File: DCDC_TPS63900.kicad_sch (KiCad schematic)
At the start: 14 parts, among them U11 TPS63900

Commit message: Initial layout before routing.
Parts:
- renumbered C27 to C23, C28 to C24, C29 to C25, C30 to C26, C31 to C27, C32 to C28, C33 to C29, C34 to C30, R24 to R28, R25 to R29, R26 to R30, R27 to R31, U11 to U12

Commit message: PCB layout done, signal routing finished, power routing remaining.
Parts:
- renumbered R28 to R29, R29 to R30, R30 to R31, R31 to R32
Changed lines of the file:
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@@
 		(dnp no)
 		(fields_autoplaced yes)
-		(property "Reference" "R29"
+		(property "Reference" "R30"
 			(at 162.56 114.2999 0)
 			(show_name no)
@@
 			(project "DigiFur-Rev1.0"
 				(path "/47dbac06-588f-419b-91d0-b3790df884b4/3218340f-e986-4868-8421-14e8efd0ba88"
-					(reference "R29")
-					(unit 1)
-				)
-				(path "/47dbac06-588f-419b-91d0-b3790df884b4/88e4d8d5-9b78-4fb5-9f90-e7a9602950c7"
-					(reference "R37")
-					(unit 1)
-				)
-				(path "/47dbac06-588f-419b-91d0-b3790df884b4/a83537bf-b40b-4f0e-8d76-5aa1105fd7e8"
-					(reference "R33")
-					(unit 1)
-				)
-				(path "/47dbac06-588f-419b-91d0-b3790df884b4/b9f26843-1012-4a63-8c48-45d26c73c917"
-					(reference "R41")
+					(reference "R30")
+					(unit 1)
+				)
+				(path "/47dbac06-588f-419b-91d0-b3790df884b4/88e4d8d5-9b78-4fb5-9f90-e7a9602950c7"
+					(reference "R38")
+					(unit 1)
+				)
+				(path "/47dbac06-588f-419b-91d0-b3790df884b4/a83537bf-b40b-4f0e-8d76-5aa1105fd7e8"
+					(reference "R34")
+					(unit 1)
+				)
+				(path "/47dbac06-588f-419b-91d0-b3790df884b4/b9f26843-1012-4a63-8c48-45d26c73c917"
+					(reference "R42")
 					(unit 1)
 				)
@@
 		(dnp no)
 		(fields_autoplaced yes)
-		(property "Reference" "#PWR052"
+		(property "Reference" "#PWR053"
 			(at 142.24 129.54 0)
 			(hide yes)
@@
 			(project "DigiFur-Rev1.0"
 				(path "/47dbac06-588f-419b-91d0-b3790df884b4/3218340f-e986-4868-8421-14e8efd0ba88"
-					(reference "#PWR052")
-					(unit 1)
-				)
-				(path "/47dbac06-588f-419b-91d0-b3790df884b4/88e4d8d5-9b78-4fb5-9f90-e7a9602950c7"
+					(reference "#PWR053")
+					(unit 1)
+				)
+				(path "/47dbac06-588f-419b-91d0-b3790df884b4/88e4d8d5-9b78-4fb5-9f90-e7a9602950c7"
+					(reference "#PWR055")
+					(unit 1)
+				)
+				(path "/47dbac06-588f-419b-91d0-b3790df884b4/a83537bf-b40b-4f0e-8d76-5aa1105fd7e8"
 					(reference "#PWR054")
 					(unit 1)
 				)
-				(path "/47dbac06-588f-419b-91d0-b3790df884b4/a83537bf-b40b-4f0e-8d76-5aa1105fd7e8"
-					(reference "#PWR053")
-					(unit 1)
-				)
-				(path "/47dbac06-588f-419b-91d0-b3790df884b4/b9f26843-1012-4a63-8c48-45d26c73c917"
-					(reference "#PWR055")
+				(path "/47dbac06-588f-419b-91d0-b3790df884b4/b9f26843-1012-4a63-8c48-45d26c73c917"
+					(reference "#PWR056")
 					(unit 1)
 				)
@@
 		(dnp yes)
 		(fields_autoplaced yes)
-		(property "Reference" "R30"
+		(property "Reference" "R31"
 			(at 172.72 104.1399 0)
 			(show_name no)
@@
 			(project "DigiFur-Rev1.0"
 				(path "/47dbac06-588f-419b-91d0-b3790df884b4/3218340f-e986-4868-8421-14e8efd0ba88"
-					(reference "R30")
-					(unit 1)
-				)
-				(path "/47dbac06-588f-419b-91d0-b3790df884b4/88e4d8d5-9b78-4fb5-9f90-e7a9602950c7"
-					(reference "R38")
-					(unit 1)
-				)
-				(path "/47dbac06-588f-419b-91d0-b3790df884b4/a83537bf-b40b-4f0e-8d76-5aa1105fd7e8"
-					(reference "R34")
-					(unit 1)
-				)
-				(path "/47dbac06-588f-419b-91d0-b3790df884b4/b9f26843-1012-4a63-8c48-45d26c73c917"
-					(reference "R42")
+					(reference "R31")
+					(unit 1)
+				)
+				(path "/47dbac06-588f-419b-91d0-b3790df884b4/88e4d8d5-9b78-4fb5-9f90-e7a9602950c7"
+					(reference "R39")
+					(unit 1)
+				)
+				(path "/47dbac06-588f-419b-91d0-b3790df884b4/a83537bf-b40b-4f0e-8d76-5aa1105fd7e8"
+					(reference "R35")
+					(unit 1)
+				)
+				(path "/47dbac06-588f-419b-91d0-b3790df884b4/b9f26843-1012-4a63-8c48-45d26c73c917"
+					(reference "R43")
 					(unit 1)
 				)
@@
 		(dnp no)
 		(fields_autoplaced yes)
-		(property "Reference" "R28"
+		(property "Reference" "R29"
 			(at 162.56 104.1399 0)
 			(show_name no)
@@
 			(project "DigiFur-Rev1.0"
 				(path "/47dbac06-588f-419b-91d0-b3790df884b4/3218340f-e986-4868-8421-14e8efd0ba88"
-					(reference "R28")
-					(unit 1)
-				)
-				(path "/47dbac06-588f-419b-91d0-b3790df884b4/88e4d8d5-9b78-4fb5-9f90-e7a9602950c7"
-					(reference "R36")
-					(unit 1)
-				)
-				(path "/47dbac06-588f-419b-91d0-b3790df884b4/a83537bf-b40b-4f0e-8d76-5aa1105fd7e8"
-					(reference "R32")
-					(unit 1)
-				)
-				(path "/47dbac06-588f-419b-91d0-b3790df884b4/b9f26843-1012-4a63-8c48-45d26c73c917"
-					(reference "R40")
+					(reference "R29")
+					(unit 1)
+				)
+				(path "/47dbac06-588f-419b-91d0-b3790df884b4/88e4d8d5-9b78-4fb5-9f90-e7a9602950c7"
+					(reference "R37")
+					(unit 1)
+				)
+				(path "/47dbac06-588f-419b-91d0-b3790df884b4/a83537bf-b40b-4f0e-8d76-5aa1105fd7e8"
+					(reference "R33")
+					(unit 1)
+				)
+				(path "/47dbac06-588f-419b-91d0-b3790df884b4/b9f26843-1012-4a63-8c48-45d26c73c917"
+					(reference "R41")
 					(unit 1)
 				)
@@
 		(dnp yes)
 		(fields_autoplaced yes)
-		(property "Reference" "R31"
+		(property "Reference" "R32"
 			(at 172.72 114.2999 0)
 			(show_name no)
@@
 			(project "DigiFur-Rev1.0"
 				(path "/47dbac06-588f-419b-91d0-b3790df884b4/3218340f-e986-4868-8421-14e8efd0ba88"
-					(reference "R31")
-					(unit 1)
-				)
-				(path "/47dbac06-588f-419b-91d0-b3790df884b4/88e4d8d5-9b78-4fb5-9f90-e7a9602950c7"
-					(reference "R39")
-					(unit 1)
-				)
-				(path "/47dbac06-588f-419b-91d0-b3790df884b4/a83537bf-b40b-4f0e-8d76-5aa1105fd7e8"
-					(reference "R35")
-					(unit 1)
-				)
-				(path "/47dbac06-588f-419b-91d0-b3790df884b4/b9f26843-1012-4a63-8c48-45d26c73c917"
-					(reference "R43")
-					(unit 1)
-				)
+					(reference "R32")
+					(unit 1)
+				)
+				(path "/47dbac06-588f-419b-91d0-b3790df884b4/88e4d8d5-9b78-4fb5-9f90-e7a9602950c7"
+					(reference "R40")
+					(unit 1)
+				)
+				(path "/47dbac06-588f-419b-91d0-b3790df884b4/a83537bf-b40b-4f0e-8d76-5aa1105fd7e8"
+					(reference "R36")
+					(unit 1)
+				)
+				(path "/47dbac06-588f-419b-91d0-b3790df884b4/b9f26843-1012-4a63-8c48-45d26c73c917"
+					(reference "R44")
+					(unit 1)
+				)

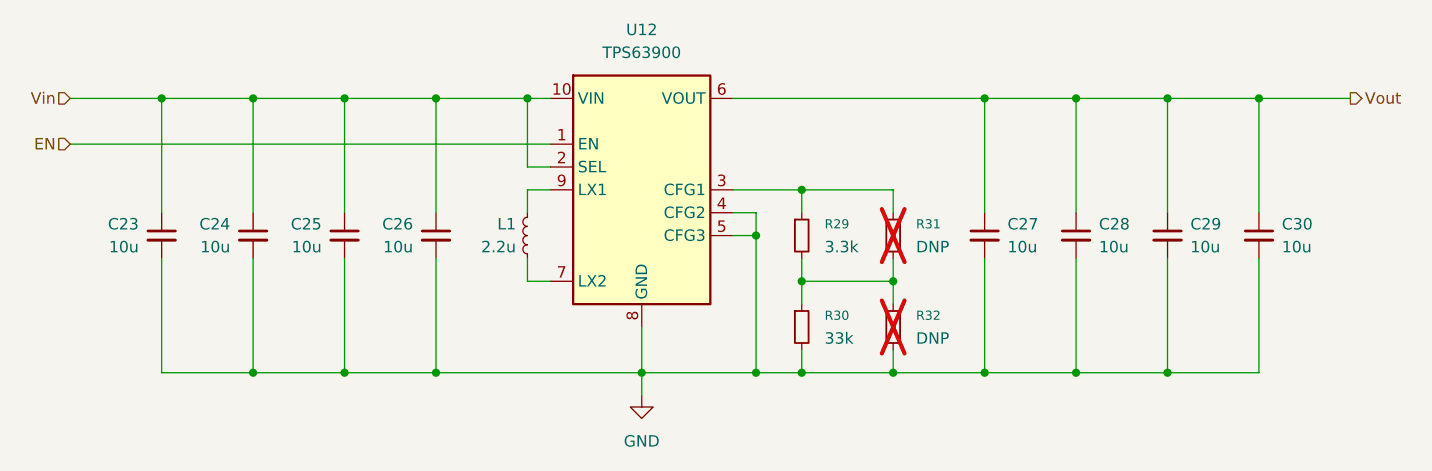
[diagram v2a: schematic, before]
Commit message: Revision to fix problems from first board fab
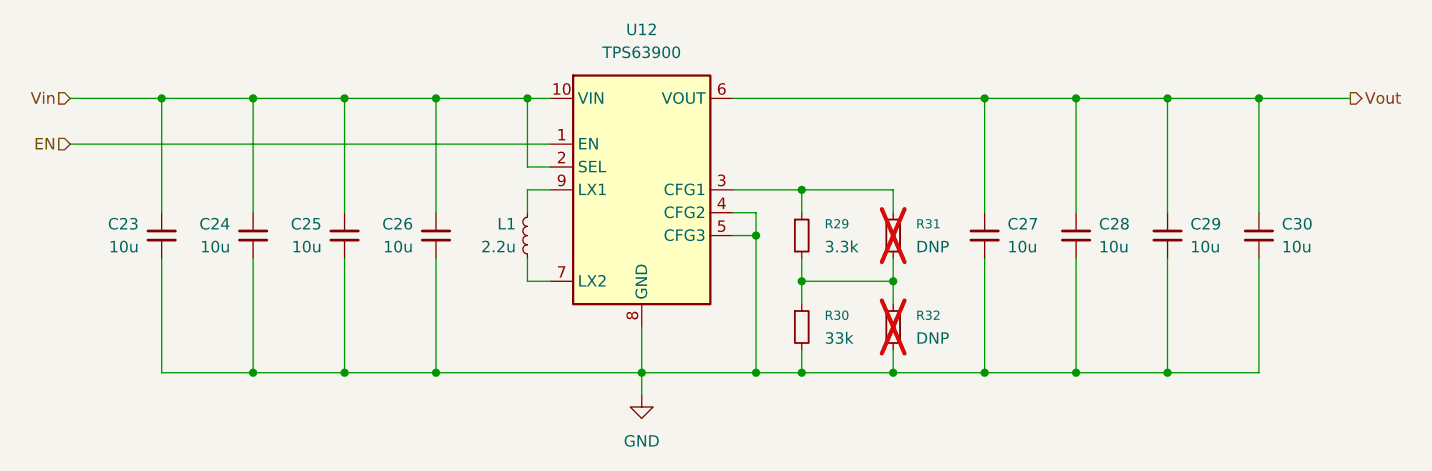
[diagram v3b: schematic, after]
